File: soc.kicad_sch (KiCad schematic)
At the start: 89 parts, among them U1 MPFS250T-FCVG484

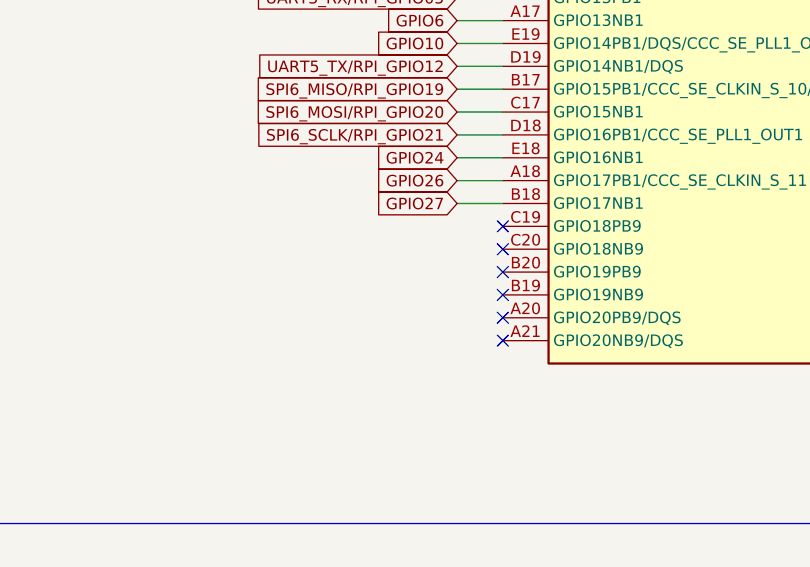
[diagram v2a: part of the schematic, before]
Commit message: [#54899] Add backup UART and SDIO to WiFi module
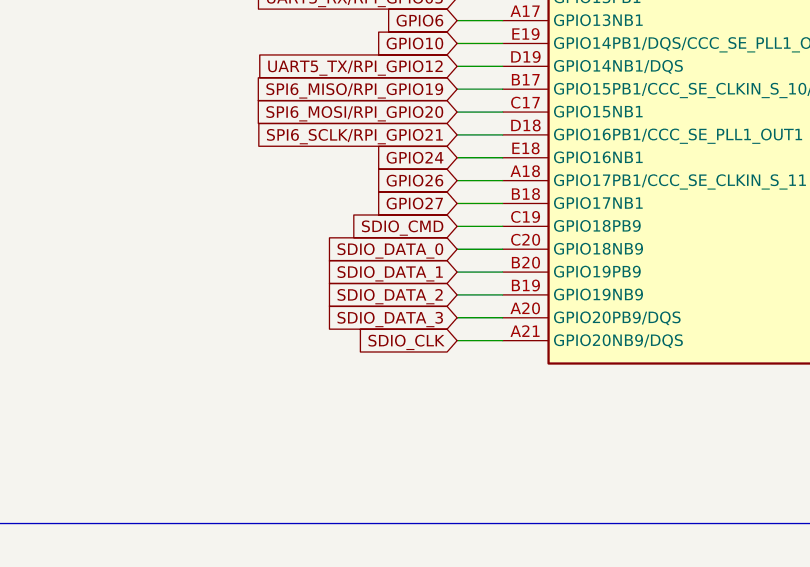
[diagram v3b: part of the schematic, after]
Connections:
- net SDIO_DATA_3: now reaches U1.A20 (GPIO20PB9/DQS)
- net SDIO_CLK: now reaches U1.A21 (GPIO20NB9/DQS)
- net SDIO_DATA_2: now reaches U1.B19 (GPIO19NB9)
- net SDIO_DATA_1: now reaches U1.B20 (GPIO19PB9)
- net SDIO_CMD: now reaches U1.C19 (GPIO18PB9)
- net SDIO_DATA_0: now reaches U1.C20 (GPIO18NB9)
- no-connect marks 54 -> 48
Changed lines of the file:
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@@
   (no_connect (at 345.44 140.97))
   (no_connect (at 345.44 57.15))
-  (no_connect (at 254 143.51))
   (no_connect (at 50.8 63.5))
   (no_connect (at 50.8 119.38))
@@
   (no_connect (at 345.44 90.17))
   (no_connect (at 140.97 121.92))
-  (no_connect (at 254 151.13))
   (no_connect (at 254 67.31))
   (no_connect (at 140.97 88.9))
@@
   (no_connect (at 140.97 68.58))
   (no_connect (at 140.97 83.82))
-  (no_connect (at 254 148.59))
   (no_connect (at 50.8 121.92))
-  (no_connect (at 254 146.05))
   (no_connect (at 140.97 86.36))
   (no_connect (at 254 102.87))
@@
   (no_connect (at 140.97 99.06))
   (no_connect (at 140.97 78.74))
-  (no_connect (at 254 140.97))
   (no_connect (at 50.8 111.76))
-  (no_connect (at 254 138.43))
   (no_connect (at 254 97.79))
   (no_connect (at 140.97 111.76))
@@
     (stroke (width 0) (type default))
   )
+  (wire (pts (xy 248.92 146.05) (xy 254 146.05))
+    (stroke (width 0) (type default))
+  )
   (wire (pts (xy 45.72 68.58) (xy 50.8 68.58))
     (stroke (width 0) (type default))
@@
     (stroke (width 0) (type default))
   )
+  (wire (pts (xy 248.92 138.43) (xy 254 138.43))
+    (stroke (width 0) (type default))
+  )
   (wire (pts (xy 238.76 57.15) (xy 254 57.15))
     (stroke (width 0) (type default))
@@
     (stroke (width 0) (type default))
   )
+  (wire (pts (xy 248.92 151.13) (xy 254 151.13))
+    (stroke (width 0) (type default))
+  )
   (wire (pts (xy 73.66 222.25) (xy 73.66 223.52))
     (stroke (width 0) (type default))
@@
     (stroke (width 0) (type default))
   )
+  (wire (pts (xy 248.92 143.51) (xy 254 143.51))
+    (stroke (width 0) (type default))
+  )
   (wire (pts (xy 347.98 41.91) (xy 347.98 46.99))
     (stroke (width 0) (type default))
@@
     (stroke (width 0) (type default))
   )
+  (wire (pts (xy 248.92 148.59) (xy 254 148.59))
+    (stroke (width 0) (type default))
+  )
   (wire (pts (xy 127 223.52) (xy 137.16 223.52))
     (stroke (width 0) (type default))
@@
     (stroke (width 0) (type default))
   )
+  (wire (pts (xy 248.92 140.97) (xy 254 140.97))
+    (stroke (width 0) (type default))
+  )
   (wire (pts (xy 162.56 215.9) (xy 162.56 217.17))
     (stroke (width 0) (type default))
@@
     )
   )
+  (global_label "SDIO_DATA_2" (shape input) (at 248.92 146.05 180) (fields_autoplaced)
+    (effects (font (size 1.27 1.27)) (justify right))
+    (property "Intersheetrefs" "${INTERSHEET_REFS}" (at 233.9605 146.05 0)
+      (effects (font (size 1.27 1.27)) (justify right) hide)
+    )
+  )
   (global_label "Crosslink_D3" (shape input) (at 45.72 73.66 180) (fields_autoplaced)
     (effects (font (size 1.27 1.27)) (justify right))
@@
     )
   )
+  (global_label "SDIO_DATA_0" (shape input) (at 248.92 140.97 180) (fields_autoplaced)
+    (effects (font (size 1.27 1.27)) (justify right))
+    (property "Intersheetrefs" "${INTERSHEET_REFS}" (at 233.9605 140.97 0)
+      (effects (font (size 1.27 1.27)) (justify right) hide)
+    )
+  )
   (global_label "UART5_TX{slash}RPI_GPIO12" (shape input) (at 248.92 120.65 180) (fields_autoplaced)
     (effects (font (size 1.27 1.27)) (justify right))
@@
     )
   )
+  (global_label "SDIO_CLK" (shape input) (at 248.92 151.13 180) (fields_autoplaced)
+    (effects (font (size 1.27 1.27)) (justify right))
+    (property "Intersheetrefs" "${INTERSHEET_REFS}" (at 236.9843 151.13 0)
+      (effects (font (size 1.27 1.27)) (justify right) hide)
+    )
+  )
   (global_label "Crosslink_D12" (shape input) (at 45.72 93.98 180) (fields_autoplaced)
     (effects (font (size 1.27 1.27)) (justify right))
@@
     )
   )
+  (global_label "SDIO_DATA_1" (shape input) (at 248.92 143.51 180) (fields_autoplaced)
+    (effects (font (size 1.27 1.27)) (justify right))
+    (property "Intersheetrefs" "${INTERSHEET_REFS}" (at 233.9605 143.51 0)
+      (effects (font (size 1.27 1.27)) (justify right) hide)
+    )
+  )
   (global_label "PAC1934_SCL" (shape input) (at 350.52 128.27 0) (fields_autoplaced)
     (effects (font (size 1.27 1.27)) (justify left))
@@
     )
   )
+  (global_label "SDIO_DATA_3" (shape input) (at 248.92 148.59 180) (fields_autoplaced)
+    (effects (font (size 1.27 1.27)) (justify right))
+    (property "Intersheetrefs" "${INTERSHEET_REFS}" (at 233.9605 148.59 0)
+      (effects (font (size 1.27 1.27)) (justify right) hide)
+    )
+  )
   (global_label "VDDAUX" (shape input) (at 233.68 229.87 180) (fields_autoplaced)
     (effects (font (size 1.27 1.27)) (justify right))
@@
     )
   )
+  (global_label "SDIO_CMD" (shape input) (at 248.92 138.43 180) (fields_autoplaced)
+    (effects (font (size 1.27 1.27)) (justify right))
+    (property "Intersheetrefs" "${INTERSHEET_REFS}" (at 236.561 138.43 0)
+      (effects (font (size 1.27 1.27)) (justify right) hide)
+    )
+  )

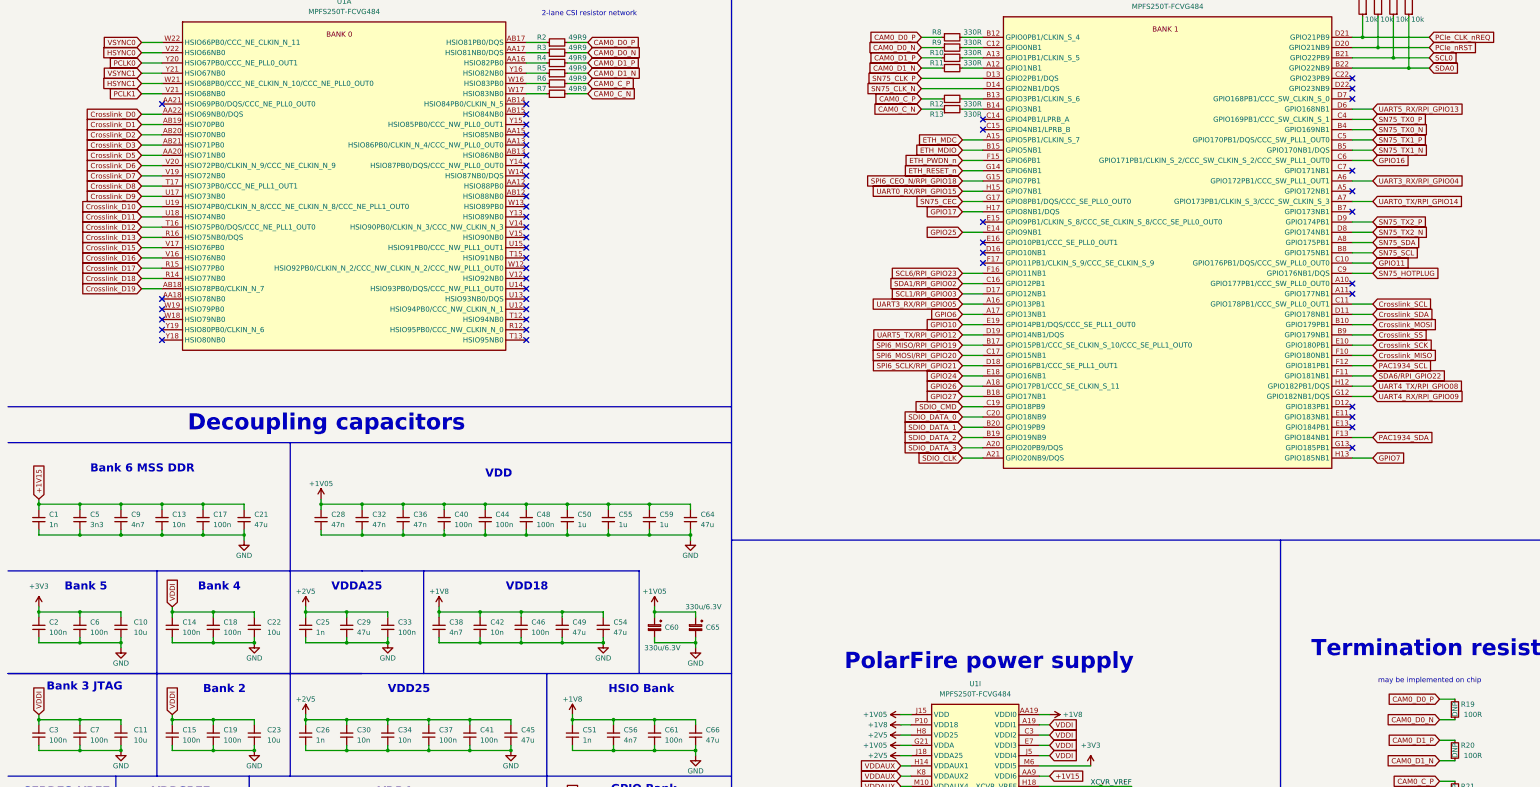
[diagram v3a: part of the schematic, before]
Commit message: [#55197] Connect HDMI to PF Bank 1
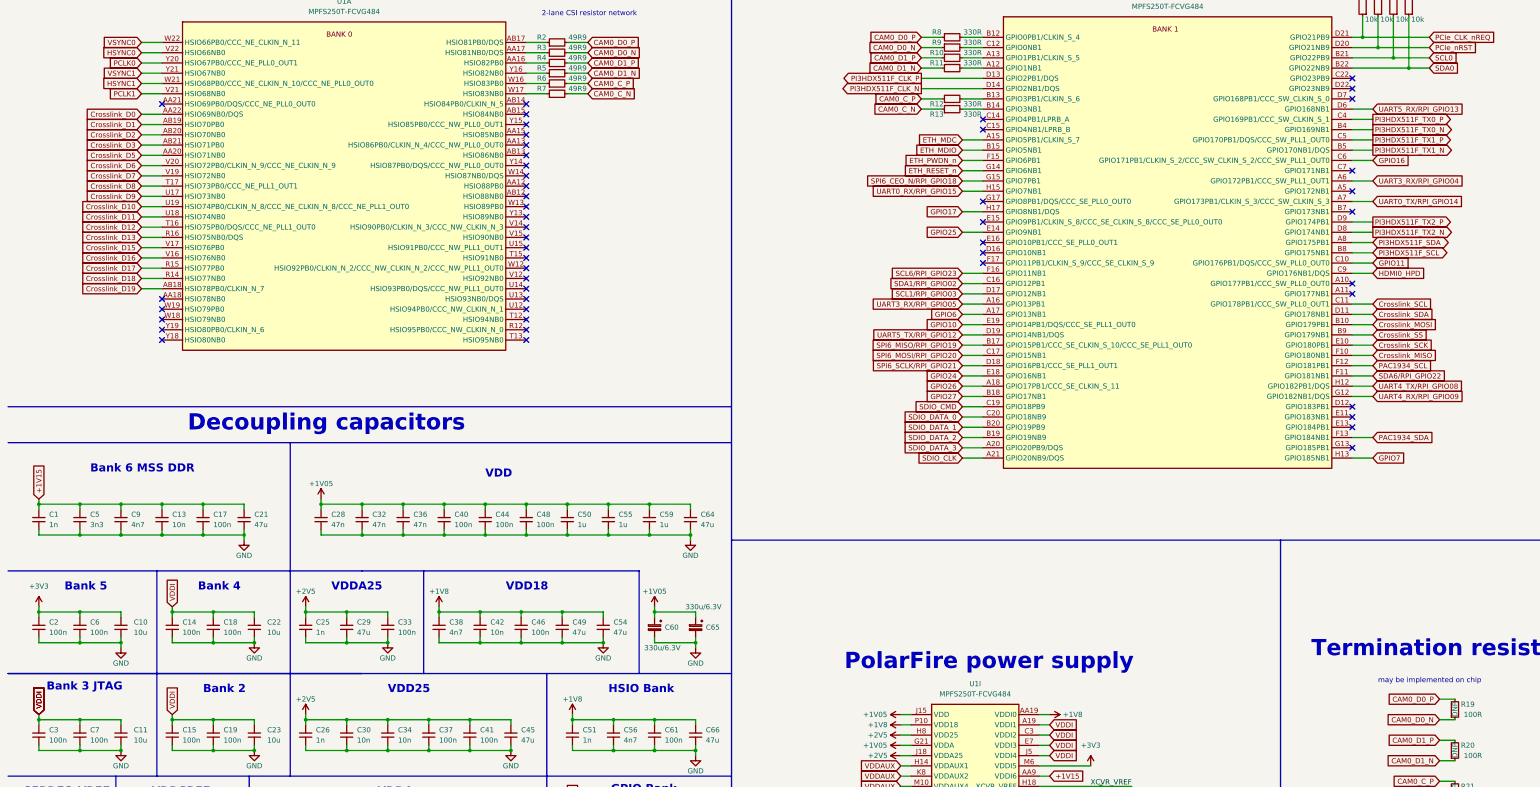
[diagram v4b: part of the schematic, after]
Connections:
- net SN75_CEC: no longer names the net of U1.G17 (GPIO8PB1/DQS/CCC_SE_PLL0_OUT0)
- net SN75_CLK_N renamed PI3HDX511F_CLK_N
- net SN75_CLK_P renamed PI3HDX511F_CLK_P
- net SN75_HOTPLUG renamed HDMI0_HPD
- net SN75_SCL renamed PI3HDX511F_SCL
- net SN75_SDA renamed PI3HDX511F_SDA
- net SN75_TX0_N renamed PI3HDX511F_TX0_N
- net SN75_TX0_P renamed PI3HDX511F_TX0_P
- net SN75_TX1_N renamed PI3HDX511F_TX1_N
- net SN75_TX1_P renamed PI3HDX511F_TX1_P
- net SN75_TX2_N renamed PI3HDX511F_TX2_N
- net SN75_TX2_P renamed PI3HDX511F_TX2_P
- no-connect marks 48 -> 49
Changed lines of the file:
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@@
   (no_connect (at 140.97 101.6))
   (no_connect (at 254 100.33))
+  (no_connect (at 254 87.63))
   (no_connect (at 345.44 62.23))
   (no_connect (at 140.97 119.38))
@@
     (stroke (width 0) (type default))
   )
-  (wire (pts (xy 248.92 87.63) (xy 254 87.63))
-    (stroke (width 0) (type default))
-  )
   (wire (pts (xy 30.48 189.23) (xy 30.48 190.5))
     (stroke (width 0) (type default))
@@
     )
   )
-  (global_label "SN75_TX0_P" (shape input) (at 350.52 67.31 0) (fields_autoplaced)
+  (global_label "PI3HDX511F_TX0_P" (shape output) (at 350.52 67.31 0) (fields_autoplaced)
     (effects (font (size 1.27 1.27)) (justify left))
-    (property "Intersheetrefs" "${INTERSHEET_REFS}" (at 365.056 67.31 0)
+    (property "Intersheetrefs" "${INTERSHEET_REFS}" (at 371.7084 67.31 0)
       (effects (font (size 1.27 1.27)) (justify left) hide)
     )
@@
     )
   )
-  (global_label "SN75_TX1_P" (shape input) (at 350.52 72.39 0) (fields_autoplaced)
+  (global_label "PI3HDX511F_TX1_P" (shape output) (at 350.52 72.39 0) (fields_autoplaced)
     (effects (font (size 1.27 1.27)) (justify left))
-    (property "Intersheetrefs" "${INTERSHEET_REFS}" (at 365.056 72.39 0)
+    (property "Intersheetrefs" "${INTERSHEET_REFS}" (at 371.7084 72.39 0)
       (effects (font (size 1.27 1.27)) (justify left) hide)
     )
@@
     )
   )
-  (global_label "SN75_TX2_P" (shape input) (at 350.52 92.71 0) (fields_autoplaced)
+  (global_label "PI3HDX511F_TX2_P" (shape output) (at 350.52 92.71 0) (fields_autoplaced)
     (effects (font (size 1.27 1.27)) (justify left))
-    (property "Intersheetrefs" "${INTERSHEET_REFS}" (at 365.056 92.71 0)
+    (property "Intersheetrefs" "${INTERSHEET_REFS}" (at 371.7084 92.71 0)
       (effects (font (size 1.27 1.27)) (justify left) hide)
     )
@@
     )
   )
-  (global_label "SN75_CLK_P" (shape input) (at 238.76 57.15 180) (fields_autoplaced)
+  (global_label "PI3HDX511F_CLK_P" (shape output) (at 238.76 57.15 180) (fields_autoplaced)
     (effects (font (size 1.27 1.27)) (justify right))
-    (property "Intersheetrefs" "${INTERSHEET_REFS}" (at 224.0425 57.15 0)
+    (property "Intersheetrefs" "${INTERSHEET_REFS}" (at 217.3901 57.15 0)
       (effects (font (size 1.27 1.27)) (justify right) hide)
     )
@@
     )
   )
-  (global_label "SN75_SCL" (shape input) (at 350.52 100.33 0) (fields_autoplaced)
+  (global_label "PI3HDX511F_SCL" (shape bidirectional) (at 350.52 100.33 0) (fields_autoplaced)
     (effects (font (size 1.27 1.27)) (justify left))
-    (property "Intersheetrefs" "${INTERSHEET_REFS}" (at 362.9394 100.33 0)
+    (property "Intersheetrefs" "${INTERSHEET_REFS}" (at 370.7031 100.33 0)
       (effects (font (size 1.27 1.27)) (justify left) hide)
     )
@@
     )
   )
-  (global_label "SN75_CLK_N" (shape input) (at 238.76 59.69 180) (fields_autoplaced)
+  (global_label "PI3HDX511F_CLK_N" (shape output) (at 238.76 59.69 180) (fields_autoplaced)
     (effects (font (size 1.27 1.27)) (justify right))
-    (property "Intersheetrefs" "${INTERSHEET_REFS}" (at 223.982 59.69 0)
+    (property "Intersheetrefs" "${INTERSHEET_REFS}" (at 217.3296 59.69 0)
       (effects (font (size 1.27 1.27)) (justify right) hide)
     )
   )
-  (global_label "SN75_TX0_N" (shape input) (at 350.52 69.85 0) (fields_autoplaced)
+  (global_label "PI3HDX511F_TX0_N" (shape output) (at 350.52 69.85 0) (fields_autoplaced)
     (effects (font (size 1.27 1.27)) (justify left))
-    (property "Intersheetrefs" "${INTERSHEET_REFS}" (at 365.1165 69.85 0)
+    (property "Intersheetrefs" "${INTERSHEET_REFS}" (at 371.7689 69.85 0)
       (effects (font (size 1.27 1.27)) (justify left) hide)
     )
@@
     )
   )
-  (global_label "SN75_CEC" (shape input) (at 248.92 87.63 180) (fields_autoplaced)
-    (effects (font (size 1.27 1.27)) (justify right))
-    (property "Intersheetrefs" "${INTERSHEET_REFS}" (at 236.3192 87.63 0)
-      (effects (font (size 1.27 1.27)) (justify right) hide)
-    )
-  )
   (global_label "CAM0_D0_P" (shape input) (at 367.03 210.82 180) (fields_autoplaced)
     (effects (font (size 1.27 1.27)) (justify right))
@@
     )
   )
-  (global_label "SN75_TX1_N" (shape input) (at 350.52 74.93 0) (fields_autoplaced)
+  (global_label "PI3HDX511F_TX1_N" (shape output) (at 350.52 74.93 0) (fields_autoplaced)
     (effects (font (size 1.27 1.27)) (justify left))
-    (property "Intersheetrefs" "${INTERSHEET_REFS}" (at 365.1165 74.93 0)
+    (property "Intersheetrefs" "${INTERSHEET_REFS}" (at 371.7689 74.93 0)
       (effects (font (size 1.27 1.27)) (justify left) hide)
     )
@@
     )
   )
-  (global_label "SN75_TX2_N" (shape input) (at 350.52 95.25 0) (fields_autoplaced)
+  (global_label "PI3HDX511F_TX2_N" (shape output) (at 350.52 95.25 0) (fields_autoplaced)
     (effects (font (size 1.27 1.27)) (justify left))
-    (property "Intersheetrefs" "${INTERSHEET_REFS}" (at 365.1165 95.25 0)
+    (property "Intersheetrefs" "${INTERSHEET_REFS}" (at 371.7689 95.25 0)
       (effects (font (size 1.27 1.27)) (justify left) hide)
     )
@@
     )
   )
-  (global_label "SN75_HOTPLUG" (shape input) (at 350.52 105.41 0) (fields_autoplaced)
+  (global_label "HDMI0_HPD" (shape input) (at 350.52 105.41 0) (fields_autoplaced)
     (effects (font (size 1.27 1.27)) (justify left))
-    (property "Intersheetrefs" "${INTERSHEET_REFS}" (at 367.959 105.41 0)
+    (property "Intersheetrefs" "${INTERSHEET_REFS}" (at 364.2095 105.41 0)
+      (effects (font (size 1.27 1.27)) (justify left) hide)
+    )
+  )
+  (global_label "VDDI" (shape input) (at 20.32 214.63 90) (fields_autoplaced)
+    (effects (font (size 1.27 1.27)) (justify left))
+    (property "Intersheetrefs" "${INTERSHEET_REFS}" (at 20.2406 207.9836 90)
       (effects (font (size 1.27 1.27)) (justify left) hide)
     )
@@
     )
   )
-  (global_label "SN75_SDA" (shape input) (at 350.52 97.79 0) (fields_autoplaced)
+  (global_label "PI3HDX511F_SDA" (shape bidirectional) (at 350.52 97.79 0) (fields_autoplaced)
     (effects (font (size 1.27 1.27)) (justify left))
-    (property "Intersheetrefs" "${INTERSHEET_REFS}" (at 362.9999 97.79 0)
+    (property "Intersheetrefs" "${INTERSHEET_REFS}" (at 370.7636 97.79 0)
       (effects (font (size 1.27 1.27)) (justify left) hide)
     )

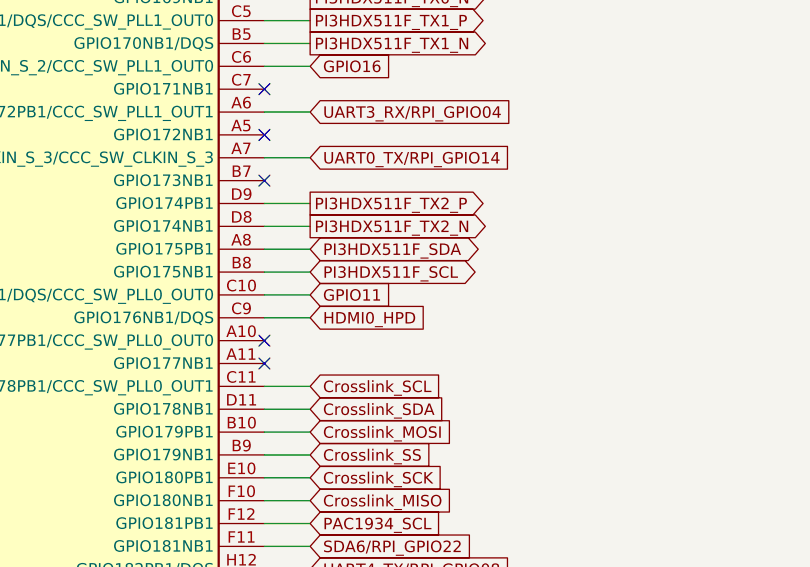
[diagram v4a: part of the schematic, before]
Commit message: [#55197] Add I2C level shifter
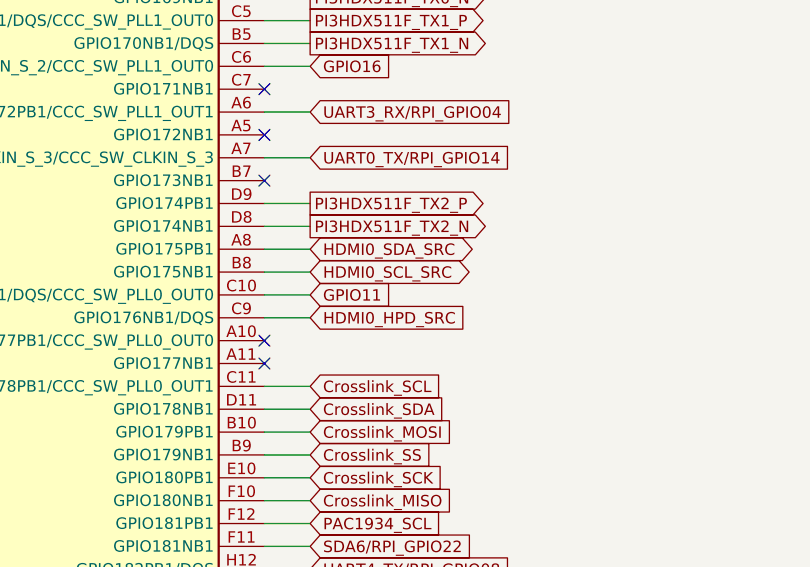
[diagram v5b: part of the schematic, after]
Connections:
- net HDMI0_HPD renamed HDMI0_HPD_SRC
- net PI3HDX511F_SCL renamed HDMI0_SCL_SRC
- net PI3HDX511F_SDA renamed HDMI0_SDA_SRC
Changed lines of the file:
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@@
     )
   )
-  (global_label "PI3HDX511F_SCL" (shape bidirectional) (at 350.52 100.33 0) (fields_autoplaced)
-    (effects (font (size 1.27 1.27)) (justify left))
-    (property "Intersheetrefs" "${INTERSHEET_REFS}" (at 370.7031 100.33 0)
+  (global_label "HDMI0_SCL_SRC" (shape bidirectional) (at 350.52 100.33 0) (fields_autoplaced)
+    (effects (font (size 1.27 1.27)) (justify left))
+    (property "Intersheetrefs" "${INTERSHEET_REFS}" (at 369.675 100.33 0)
       (effects (font (size 1.27 1.27)) (justify left) hide)
     )
@@
     )
   )
-  (global_label "HDMI0_HPD" (shape input) (at 350.52 105.41 0) (fields_autoplaced)
-    (effects (font (size 1.27 1.27)) (justify left))
-    (property "Intersheetrefs" "${INTERSHEET_REFS}" (at 364.2095 105.41 0)
+  (global_label "HDMI0_HPD_SRC" (shape input) (at 350.52 105.41 0) (fields_autoplaced)
+    (effects (font (size 1.27 1.27)) (justify left))
+    (property "Intersheetrefs" "${INTERSHEET_REFS}" (at 368.9266 105.41 0)
       (effects (font (size 1.27 1.27)) (justify left) hide)
     )
@@
     )
   )
-  (global_label "PI3HDX511F_SDA" (shape bidirectional) (at 350.52 97.79 0) (fields_autoplaced)
-    (effects (font (size 1.27 1.27)) (justify left))
-    (property "Intersheetrefs" "${INTERSHEET_REFS}" (at 370.7636 97.79 0)
-      (effects (font (size 1.27 1.27)) (justify left) hide)
-    )
+  (global_label "HDMI0_SDA_SRC" (shape bidirectional) (at 350.52 97.79 0) (fields_autoplaced)
+    (effects (font (size 1.27 1.27)) (justify left))
+    (property "Intersheetrefs" "${INTERSHEET_REFS}" (at 369.7355 97.79 0)
+      (effects (font (size 1.27 1.27)) (justify left) hide)
+    )
